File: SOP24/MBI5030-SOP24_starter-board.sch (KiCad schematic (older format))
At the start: 43 parts, among them IC1 MADW__MBI5030GF/GTS, P1 CONN_1, P2 CONN_1, P3 CONN_12, P4 CONN_12, P5 CONN_1, P6 CONN_1

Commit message: First doodles.
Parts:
- removed P1, P2, P5, P6: CONN_1, symbol CONN_1
- added JP1: int. LEDs, symbol JUMPER
- C1: value C -> 100nF
- C2: value C -> 4.7µF
- IC1: value MADW__MBI5030GF/GTS -> MBI5030GF
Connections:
- net OUT0: no longer D9.2 (K)
- net OUT1: no longer D10.2 (K)
- net OUT10: now also D11.2 (K)
- net OUT11: now also D12.2 (K)
- net OUT12: now also D13.2 (K)
- net OUT13: now also D14.2 (K)
- net OUT14: now also D15.2 (K)
- net OUT15: now also D16.2 (K)
- net OUT2: no longer D11.2 (K)
- net OUT3: no longer D12.2 (K)
- net OUT4: no longer D13.2 (K)
- net OUT5: no longer D14.2 (K)
- net OUT6: no longer D15.2 (K)
- net OUT7: no longer D16.2 (K)
- net OUT8: now also D9.2 (K)
- net OUT9: now also D10.2 (K)
- net VCC: now also JP1.1; no longer R1.1, R10.1, R11.1, R12.1, R13.1, R14.1, R15.1, R16.1, R2.1, R3.1, R4.1, R5.1, R6.1, R7.1, R8.1, R9.1
- new net: JP1.2, R1.1, R10.1, R11.1, R12.1, R13.1, R14.1, R15.1, R16.1, R2.1, R3.1, R4.1, R5.1, R6.1, R7.1, R8.1, R9.1
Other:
- note added: "Disconnect before powering\nexternal LEDs!"
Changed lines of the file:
@@
-EESchema Schematic File Version 2  date Sun 20 Jan 2013 08:10:18 PM CET
+EESchema Schematic File Version 2  date Mon 21 Jan 2013 01:01:47 AM CET
 LIBS:my_parts
 LIBS:power
@@
 Sheet 1 1
 Title "MBI5030-SOP24_starter-board"
-Date "20 jan 2013"
+Date "21 jan 2013"
 Rev "1.00"
 Comp "2013 - blog.spitzenpfeil.org"
@@
 Wire Wire Line
 	3100 1400 3100 1350
-Wire Wire Line
-	3100 1800 3100 1850
-Wire Wire Line
-	3450 1800 3450 1850
 Wire Wire Line
 	3650 1800 3650 2000
@@
 $EndComp
 $Comp
-L CONN_1 P6
-U 1 1 5042646A
-P 3450 2000
-F 0 "P6" H 3530 2000 40  0000 L CNN
-F 1 "CONN_1" H 3450 2055 30  0001 C CNN
-	1    3450 2000
-	0    1    1    0
-$EndComp
-$Comp
-L CONN_1 P5
-U 1 1 50426467
-P 3100 2000
-F 0 "P5" H 3180 2000 40  0000 L CNN
-F 1 "CONN_1" H 3100 2055 30  0001 C CNN
-	1    3100 2000
-	0    1    1    0
-$EndComp
-$Comp
-L CONN_1 P2
-U 1 1 50426464
-P 3450 1200
-F 0 "P2" H 3530 1200 40  0000 L CNN
-F 1 "CONN_1" H 3450 1255 30  0001 C CNN
-	1    3450 1200
-	0    -1   -1   0
-$EndComp
-$Comp
-L CONN_1 P1
-U 1 1 5042645F
-P 3100 1200
-F 0 "P1" H 3180 1200 40  0000 L CNN
-F 1 "CONN_1" H 3100 1255 30  0001 C CNN
-	1    3100 1200
-	0    -1   -1   0
-$EndComp
-$Comp
 L C C2
 U 1 1 50426447
 P 3450 1600
 F 0 "C2" H 3500 1700 50  0000 L CNN
-F 1 "C" H 3500 1500 50  0000 L CNN
+F 1 "4.7µF" H 3500 1500 50  0000 L CNN
 	1    3450 1600
 	1    0    0    -1
@@
 P 3100 1600
 F 0 "C1" H 3150 1700 50  0000 L CNN
-F 1 "C" H 3150 1500 50  0000 L CNN
+F 1 "100nF" H 3150 1500 50  0000 L CNN
 	1    3100 1600
 	1    0    0    -1
@@
 P 2000 3600
 F 0 "IC1" H 2000 4050 60  0000 C CNN
-F 1 "MADW__MBI5030GF/GTS" H 2000 4200 60  0000 C CNN
+F 1 "MBI5030GF" H 2000 4200 60  0000 C CNN
 	1    2000 3600
 	1    0    0    -1
@@
 $EndComp
 Text Label 4700 3500 3    60   ~ 0
-OUT0
+OUT8
 Text Label 5000 3500 3    60   ~ 0
-OUT1
+OUT9
 Text Label 5300 3500 3    60   ~ 0
-OUT2
+OUT10
 Text Label 5600 3500 3    60   ~ 0
-OUT3
+OUT11
 Text Label 5900 3500 3    60   ~ 0
-OUT4
+OUT12
 Text Label 6200 3500 3    60   ~ 0
-OUT5
+OUT13
 Text Label 6500 3500 3    60   ~ 0
-OUT6
+OUT14
 Text Label 6800 3500 3    60   ~ 0
-OUT7
+OUT15
 Wire Wire Line
 	4700 3050 4700 3100
@@
 Connection ~ 5600 1100
 Wire Wire Line
-	4700 1100 6800 1100
+	4700 1100 6950 1100
 Connection ~ 6200 1100
 Connection ~ 6500 1100
 Wire Wire Line
-	4700 2550 6800 2550
+	4700 2550 6950 2550
 Connection ~ 5000 2550
 Connection ~ 5300 2550
@@
 L VCC #PWR08
 U 1 1 50FC3A98
-P 4700 1100
-F 0 "#PWR08" H 4700 1200 30  0001 C CNN
-F 1 "VCC" H 4700 1200 30  0000 C CNN
-	1    4700 1100
-	1    0    0    -1
-$EndComp
-$Comp
-L VCC #PWR09
-U 1 1 50FC3AA7
-P 4700 2550
-F 0 "#PWR09" H 4700 2650 30  0001 C CNN
-F 1 "VCC" H 4700 2650 30  0000 C CNN
-	1    4700 2550
-	1    0    0    -1
-$EndComp
+P 4000 2550
+F 0 "#PWR08" H 4000 2650 30  0001 C CNN
+F 1 "VCC" H 4000 2650 30  0000 C CNN
+	1    4000 2550
+	0    -1   -1   0
+$EndComp
+Wire Wire Line
+	6950 2550 6950 1100
+Connection ~ 6800 1100
+Connection ~ 6800 2550
+$Comp
+L JUMPER JP1
+U 1 1 50FC8017
+P 4400 2550
+F 0 "JP1" H 4400 2700 60  0000 C CNN
+F 1 "int. LEDs" H 4400 2470 40  0000 C CNN
+	1    4400 2550
+	1    0    0    -1
+$EndComp
+Wire Wire Line
+	4100 2550 4000 2550
+Text Notes 3300 2800 0    60   ~ 0
+Disconnect before powering\nexternal LEDs!
 $EndSCHEMATC

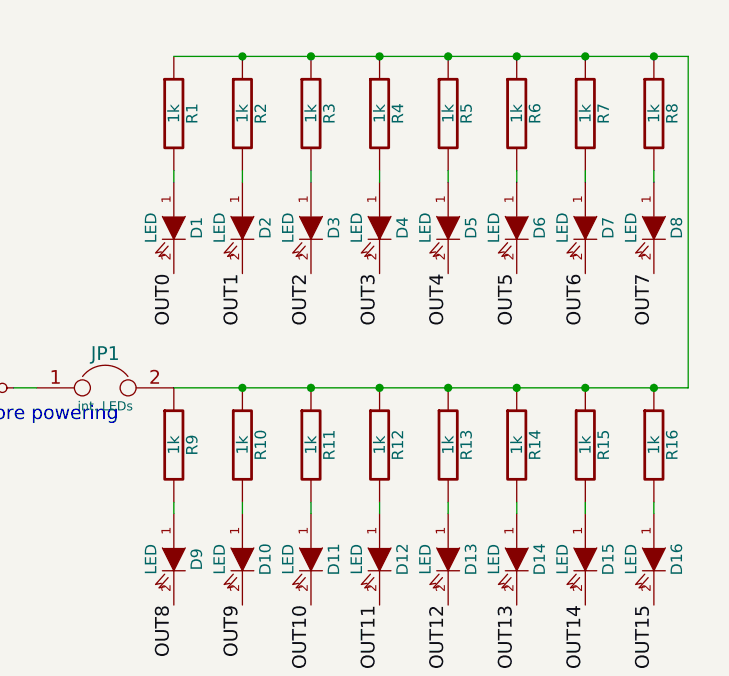
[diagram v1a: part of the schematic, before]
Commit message: Replaced 0603 resistors with 1206 4x resistor packs.
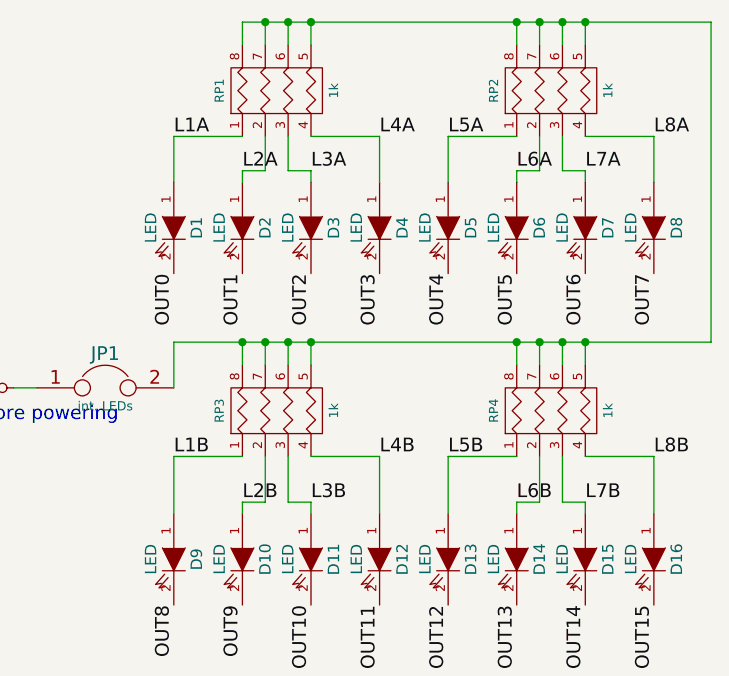
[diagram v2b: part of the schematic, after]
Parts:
- removed R1, R10, R11, R12, R13, R14, R15, R16, R2, R3, R4, R5, R6, R7, R8, R9: 1k, symbol R
- added RP1, RP2, RP3, RP4: 1k, symbol R_PACK4
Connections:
- net at JP1.2: now also RP1.5 (R4), RP1.6 (R3), RP1.7 (R2), RP1.8 (R1), RP2.5 (R4), RP2.6 (R3), RP2.7 (R2), RP2.8 (R1), RP3.5 (R4), RP3.6 (R3), RP3.7 (R2), RP3.8 (R1), RP4.5 (R4), RP4.6 (R3), RP4.7 (R2), RP4.8 (R1)
- net L1A: now reaches D1.1 (A)
- net L1A: now also RP1.1 (P1)
- net L2A: now reaches D2.1 (A)
- net L2A: now also RP1.2 (P2)
- net L4A: now reaches D4.1 (A)
- net L4A: now also RP1.4 (P4)
- net L3A: now reaches D3.1 (A)
- net L3A: now also RP1.3 (P3)
- net L5A: now reaches D5.1 (A)
- net L5A: now also RP2.1 (P1)
- net L6A: now reaches D6.1 (A)
- net L6A: now also RP2.2 (P2)
- net L7A: now reaches D7.1 (A)
- net L7A: now also RP2.3 (P3)
- net L8A: now reaches D8.1 (A)
- net L8A: now also RP2.4 (P4)
- net L1B: now reaches D9.1 (A)
- net L1B: now also RP3.1 (P1)
- net L2B: now reaches D10.1 (A)
- net L2B: now also RP3.2 (P2)
- net L4B: now reaches D12.1 (A)
- net L4B: now also RP3.4 (P4)
- net L3B: now reaches D11.1 (A)
- net L3B: now also RP3.3 (P3)
- net L5B: now reaches D13.1 (A)
- net L5B: now also RP4.1 (P1)
- net L6B: now reaches D14.1 (A)
- net L6B: now also RP4.2 (P2)
- net L7B: now reaches D15.1 (A)
- net L7B: now also RP4.3 (P3)
- net L8B: now reaches D16.1 (A)
- net L8B: now also RP4.4 (P4)

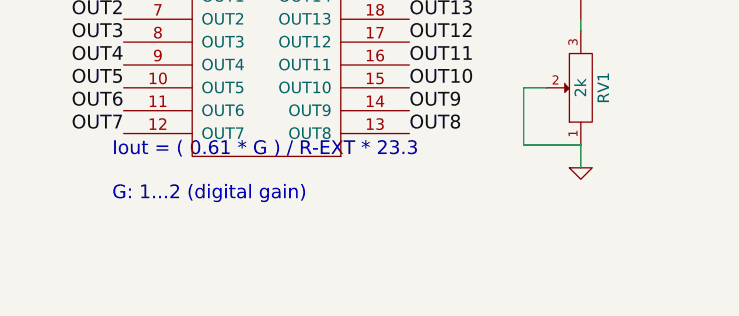
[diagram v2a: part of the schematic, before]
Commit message: Added formula to calculate a SAFE R-EXT.
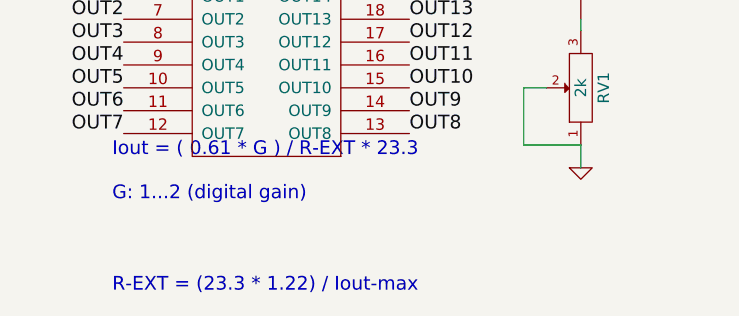
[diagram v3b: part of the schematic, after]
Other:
- note added: "R-EXT = (23.3 * 1.22) / Iout-max"
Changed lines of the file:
@@
-EESchema Schematic File Version 2  date Thu 04 Apr 2013 12:23:57 AM CEST
+EESchema Schematic File Version 2  date Mon 22 Apr 2013 03:28:40 PM CEST
 LIBS:my_parts
 LIBS:power
@@
 LIBS:valves
 LIBS:MBI5030-SOP24_starter-board-cache
-EELAYER 27 0
+EELAYER 24 0
 EELAYER END
 $Descr User 8268 5906
@@
 Sheet 1 1
 Title "MBI5030-SOP24_starter-board"
-Date "3 apr 2013"
+Date "22 apr 2013"
 Rev "1.1"
 Comp "2013 - blog.spitzenpfeil.org"
@@
 Text Label 6800 2850 0    60   ~ 0
 L8B
+Text Notes 1350 5150 0    60   ~ 0
+R-EXT = (23.3 * 1.22) / Iout-max
 $EndSCHEMATC
